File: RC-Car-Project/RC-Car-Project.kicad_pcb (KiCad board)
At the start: 4 copper layers, 80 x 120 mm, 173 parts, among them J1 Conn_01x02_Pin, J10 ANT_IF, J11 Conn_01x02, J12 Conn_01x02, J13 RF_IF, J14 Conn_01x02, J15 USB4120-03-C_REVA, J16 Conn_01x02, J2 Conn_01x02_Pin, J3 Conn_01x02_Pin, J4 Conn_01x02_Pin, J5 MCU_IF, J6 Conn_01x02, J7 Conn_01x02, J8 Conn_01x02, J9 Conn_02x09_Odd_Even, Q1 BTN8982TA, Q2 BTN8982TA, Q3 BTN8982TA, Q4 BTN8982TA, Q5 PMF250XNE, Q6 PMF250XNE, Q7 PMOS, Q8 PMF250XNE, Q9 PMF250XNE, SW1 SW_Push, SW2 SW_SPDT, U1 LMR16020PDDAR, U11 LMR16030PDDA, U3 STM32H743VGTx, U4 USBLC6-2SC6, U7 INA229AQDGSRQ1, U8 ADC082S021CIMM/NOPB, U9 SN74HC244PWR, Y1 Crystal

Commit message: Fixed DRC
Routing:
- net GNDA: vias 208 -> 209
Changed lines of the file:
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@@
 	)
 	(gr_rect
+		(start 170.307 128.524)
+		(end 171.069 130.175)
+		(stroke
+			(width 0.2)
+			(type solid)
+		)
+		(fill solid)
+		(layer "F.Cu")
+		(net 1)
+	)
+	(gr_rect
 		(start 164.211 153.289)
 		(end 165.862 154.051)
@@
 		(net 2)
 	)
+	(gr_poly
+		(pts
+			(xy 113.919 64.389) (xy 124.587 64.389) (xy 124.587 73.66) (xy 113.919 73.66)
+		)
+		(stroke
+			(width 0.2)
+			(type solid)
+		)
+		(fill solid)
+		(layer "B.Cu")
+		(net 17)
+	)
+	(gr_poly
+		(pts
+			(xy 163.576 64.389) (xy 174.244 64.389) (xy 174.244 73.66) (xy 163.576 73.66)
+		)
+		(stroke
+			(width 0.2)
+			(type solid)
+		)
+		(fill solid)
+		(layer "B.Cu")
+		(net 15)
+	)
+	(gr_poly
+		(pts
+			(xy 175.514 64.389) (xy 186.182 64.389) (xy 186.182 73.66) (xy 175.514 73.66)
+		)
+		(stroke
+			(width 0.2)
+			(type solid)
+		)
+		(fill solid)
+		(layer "B.Cu")
+		(net 14)
+	)
+	(gr_poly
+		(pts
+			(xy 125.857 64.389) (xy 136.525 64.389) (xy 136.525 73.66) (xy 125.857 73.66)
+		)
+		(stroke
+			(width 0.2)
+			(type solid)
+		)
+		(fill solid)
+		(layer "B.Cu")
+		(net 16)
+	)
 	(gr_rect
 		(start 166.4335 94.488)
@@
 	)
 	(via
+		(at 150.368 117.856)
+		(size 0.6)
+		(drill 0.3)
+		(layers "F.Cu" "B.Cu")
+		(free yes)
+		(net 1)
+	)
+	(via
 		(at 171.069 110.109)
 		(size 0.6)
@@
 	)
 	(via
+		(at 170.688 128.905)
+		(size 0.6)
+		(drill 0.3)
+		(layers "F.Cu" "B.Cu")
+		(net 1)
+	)
+	(via
 		(at 179.500546 101.473)
 		(size 0.6)
@@
 	)
 	(via
-		(at 170.688 128.27)
-		(size 0.6)
-		(drill 0.3)
-		(layers "F.Cu" "B.Cu")
-		(free yes)
-		(net 1)
-	)
-	(via
 		(at 164.465 91.059)
 		(size 0.6)
@@
 	)
 	(via
-		(at 150.368 114.935)
+		(at 150.368 116.459)
 		(size 0.6)
 		(drill 0.3)
@@
 	)
 	(via
-		(at 150.368 116.459)
+		(at 152.019 116.459)
 		(size 0.6)
 		(drill 0.3)
@@
 			(pts
 				(xy 111.887 75.819) (xy 137.922 75.819) (xy 137.922 83.312) (xy 151.511 83.312) (xy 151.511 86.106)
-				(xy 162.941 86.106) (xy 162.941 75.819) (xy 184.785 75.819) (xy 184.785 91.821) (xy 111.887 91.821)
+				(xy 162.941 86.106) (xy 162.941 75.819) (xy 186.436 75.819) (xy 186.436 91.821) (xy 111.887 91.821)
 			)
 		)

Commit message: Added PCB Caps
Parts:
- C1, C4: value 10uF/50V -> 4.7uF/50V; footprint Capacitor_SMD:C_0603_1608Metric -> Capacitor_SMD:C_1210_3225Metric
- moved C1 1.99 mm to (130.6, 102.2)
- moved C5 1.78 mm to (177.8, 99.7)
- moved C6 1.78 mm to (177.8, 98.2)
- moved TP1 1.66 mm to (178.0, 95.6), turned to 90 degrees
- moved C2 1.31 mm to (127.5, 100.7), turned to 90 degrees
- moved C4 1.21 mm to (178.6, 102.1)
- moved C3 1.14 mm to (129.8, 99.8)
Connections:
- R20 pad 4: Net-(F1-Pad2) -> GND_BATT
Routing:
- net GNDA: track 39.2 -> 41.5 mm, vias 209 -> 210
- net Net-(D8-K): track 10.2 -> 11.6 mm

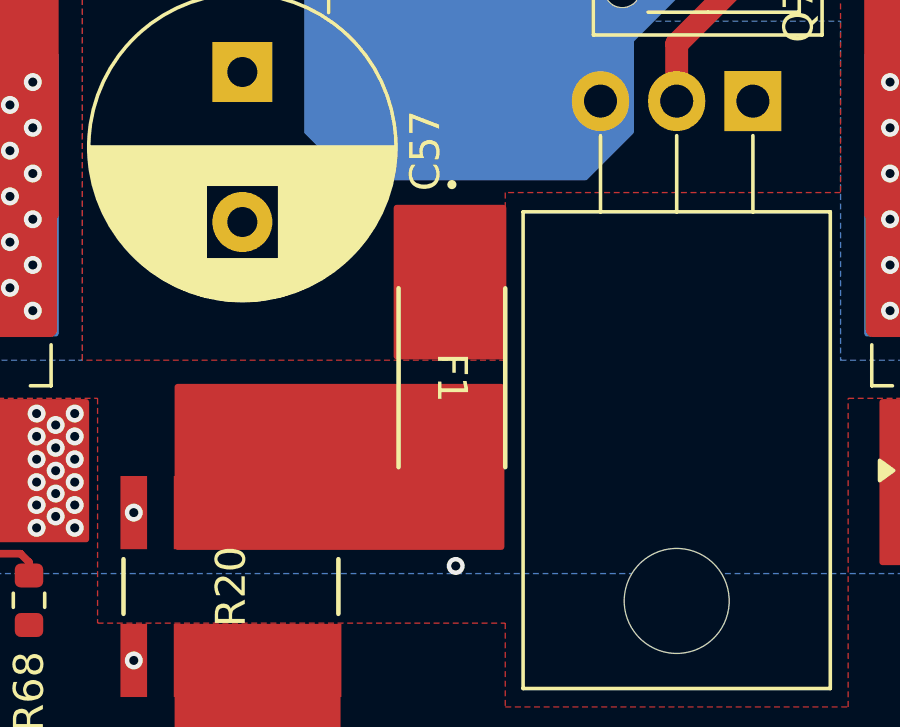
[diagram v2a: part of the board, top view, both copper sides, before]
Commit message: Re added my fuse
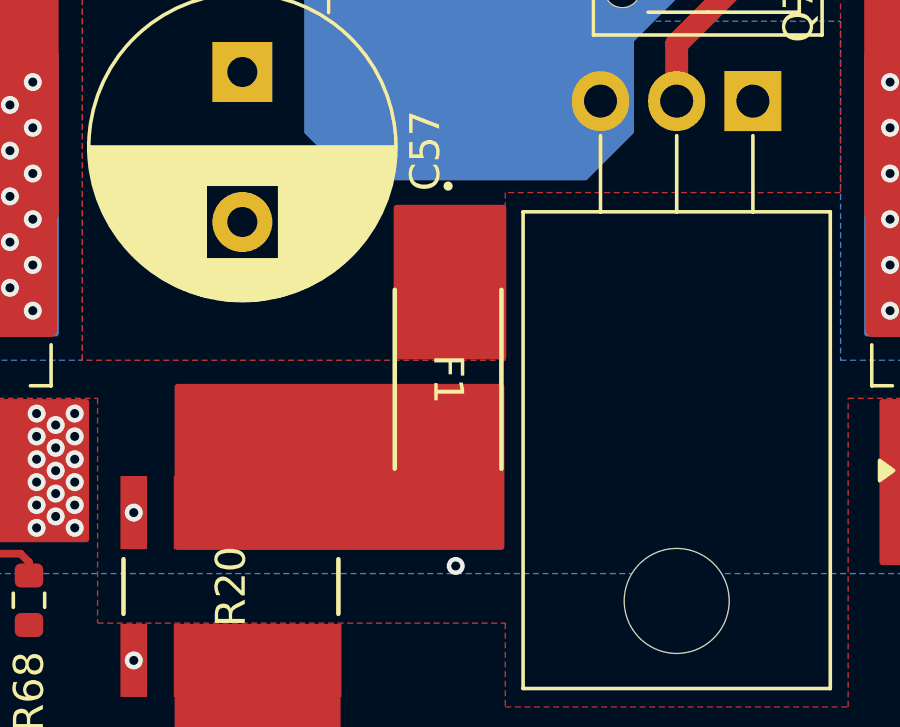
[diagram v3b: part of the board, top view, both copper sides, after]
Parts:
- moved F1 0.14 mm to (149.6, 75.2)
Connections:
- R20 pad 4: GND_BATT -> Net-(F1-Pad2)

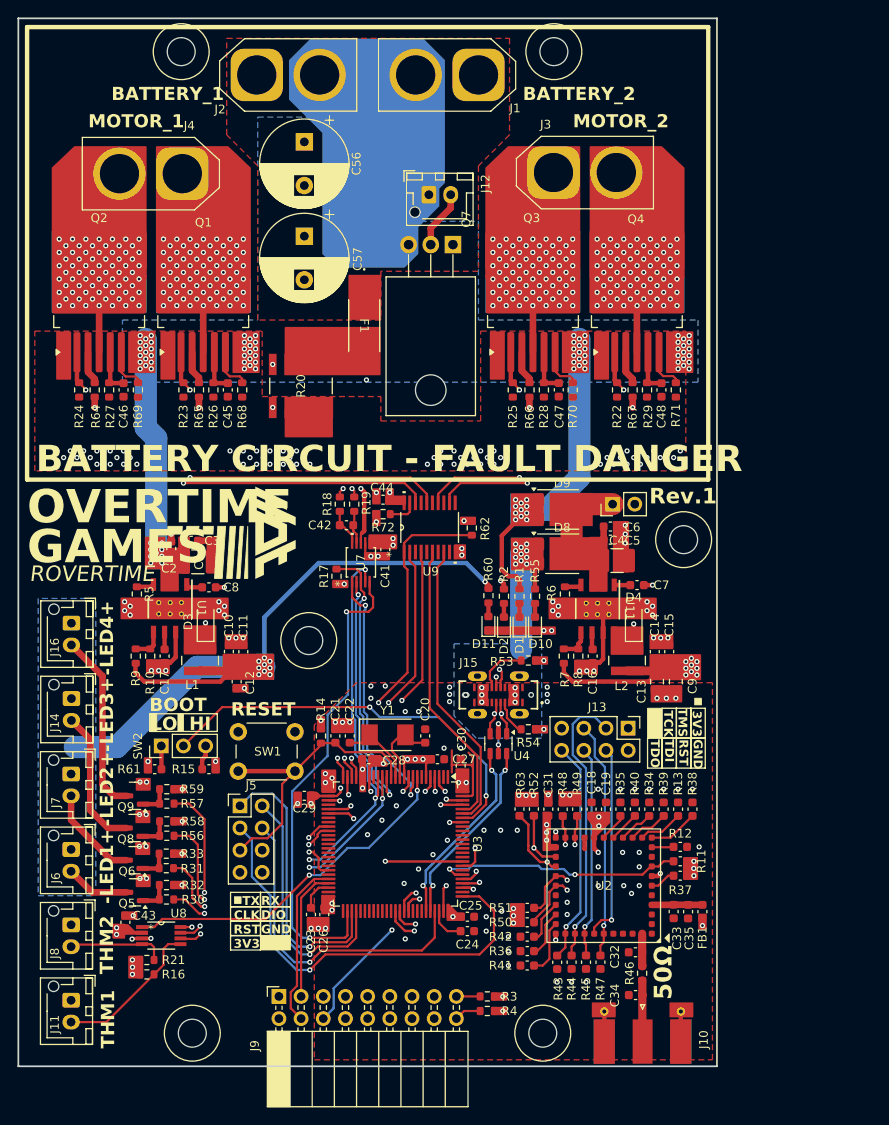
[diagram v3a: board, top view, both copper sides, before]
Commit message: Added test points, Added schematic references
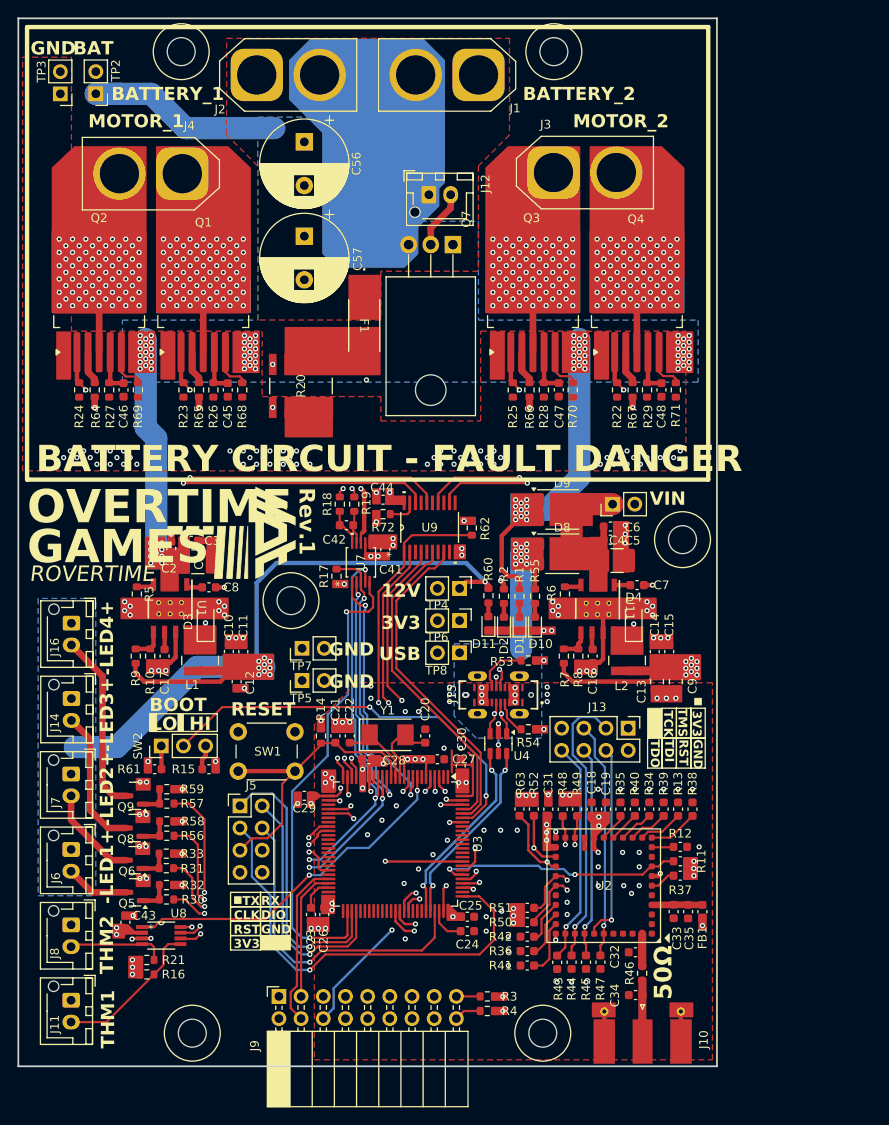
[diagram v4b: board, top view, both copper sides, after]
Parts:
- added TP2: TestPoint, Connector_PinHeader_2.54mm:PinHeader_1x02_P2.54mm_Vertical, F.Cu at (118.9, 48.6)
- added TP3: TestPoint, Connector_PinHeader_2.54mm:PinHeader_1x02_P2.54mm_Vertical, F.Cu at (114.8, 48.6)
- added TP4: TestPoint, Connector_PinHeader_2.54mm:PinHeader_1x02_P2.54mm_Vertical, F.Cu at (160.5, 105.3)
- added TP5: TestPoint, Connector_PinHeader_2.54mm:PinHeader_1x02_P2.54mm_Vertical, F.Cu at (142.5, 115.8)
- added TP6: TestPoint, Connector_PinHeader_2.54mm:PinHeader_1x02_P2.54mm_Vertical, F.Cu at (160.5, 109.0)
- added TP7: TestPoint, Connector_PinHeader_2.54mm:PinHeader_1x02_P2.54mm_Vertical, F.Cu at (142.5, 112.1)
- added TP8: TestPoint, Connector_PinHeader_2.54mm:PinHeader_1x02_P2.54mm_Vertical, F.Cu at (160.5, 112.6)
- moved REF** 5.00 mm to (141.2, 106.7)
- moved REF** 0.13 mm to (186.1, 99.7)
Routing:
- net VDD_BATT: track 78.9 -> 103.9 mm
- net +12V: track 76.6 -> 83.4 mm
- net /MCU/RIGHT_PWM2: track 33.7 -> 38.0 mm
- net /MCU/LEFT_PWM2: track 33.0 -> 36.8 mm
- net /MCU/LEFT_PWM1: track 29.4 -> 30.6 mm
- net GNDA: vias 210 -> 209
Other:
- board text added: "12V"
- board text added: "3V3"
- board text added: "BAT"
- board text added: "GND"
- board text added: "USB"
- board text added: "VIN"

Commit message: Fixed Bullshit
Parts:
- C12: value 1uF/16V -> 1uF/10V
- C19, C31, C35: value 100nF/10V -> 0.1uF/10V
- C42, C45, C46, C47, C48: value 0.1uF/25V -> 0.1uF/10V
- R16, R21: value R -> 100kohm
- R20: value WSL27262L000FEB -> 0.002 OHM
- moved R2 0.13 mm to (165.6, 106.0)
- moved R60 0.13 mm to (163.8, 106.0)
- moved R1 0.06 mm to (167.4, 106.1)
